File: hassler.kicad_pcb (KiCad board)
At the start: 2 copper layers, 86.6 x 54.6 mm, 59 parts, among them CON1 USB-MICRO-B, J1 JST, Q1 IRF510, Q2 IRF510, Q3 MMBT2222A, SW1 Off Switcher, U1 TL082, U2 TL081, U3 MCP73831, U4 LT1308

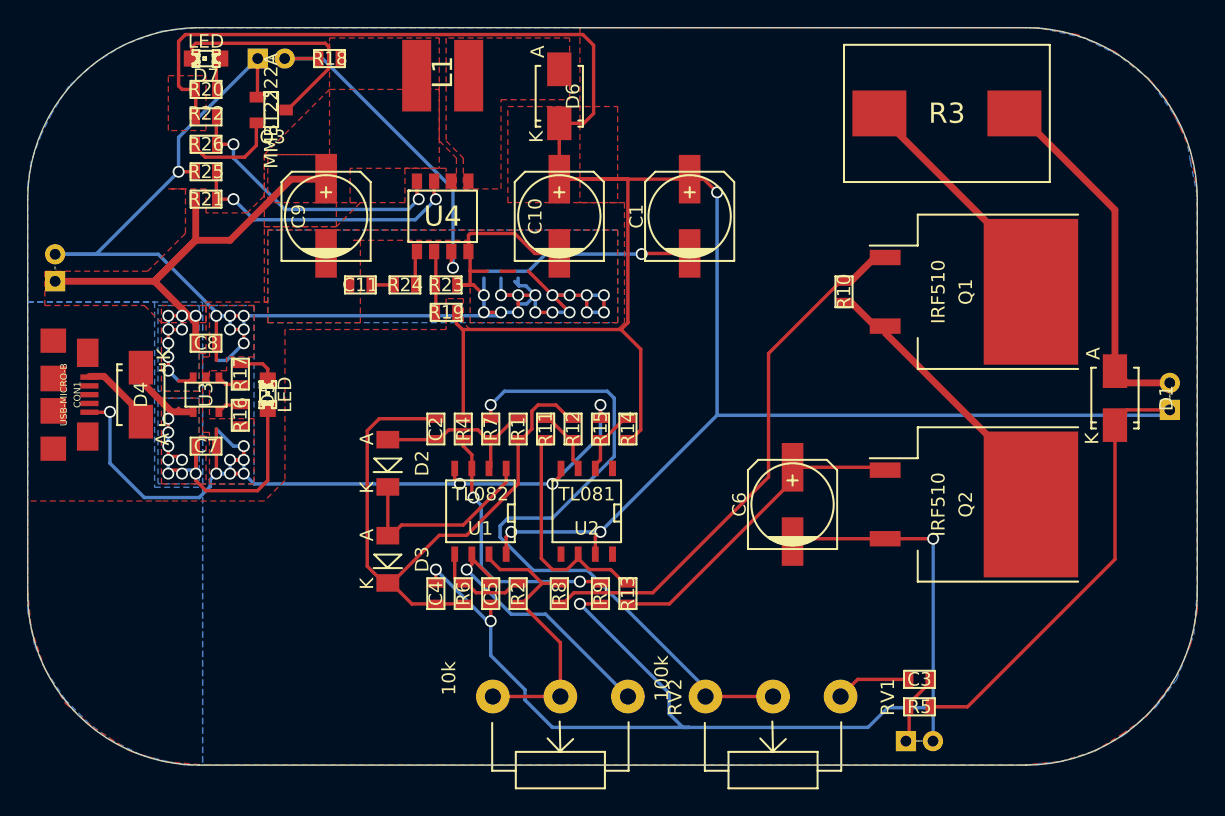
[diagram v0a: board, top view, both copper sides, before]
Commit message: Add license and OSH logo
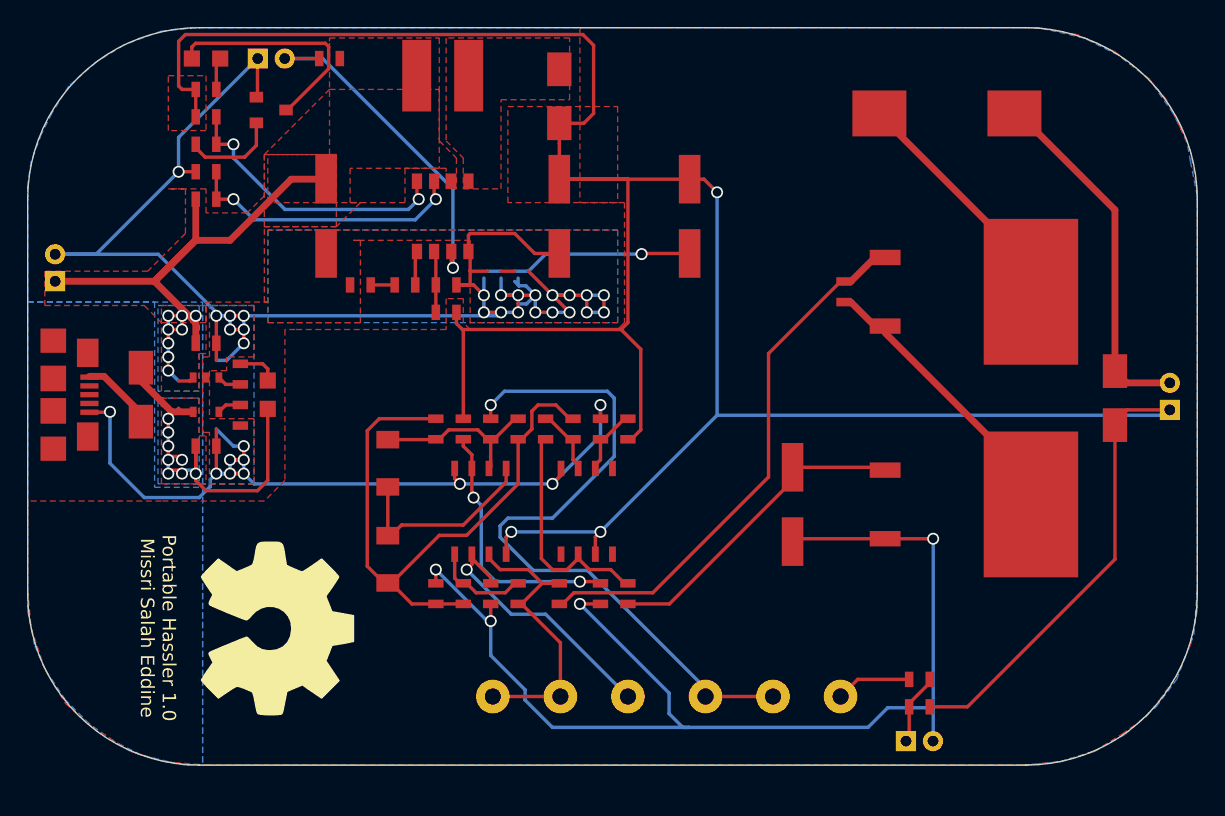
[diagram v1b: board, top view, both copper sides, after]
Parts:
- added G***: LOGO, oshw_logo:oshw_s, F.Cu at (116.8, 114.3)
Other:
- board text added: "Portable Hassler 1.0 Missri Salah Eddine"
